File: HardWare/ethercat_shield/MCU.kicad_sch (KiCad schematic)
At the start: 49 parts, among them J2 Conn_01x03, J3 Conn_01x04, J6 Conn_01x03, J7 Conn_01x04, SW1 SW_Push, U5 STM32F407VETx, U6 TJA1051T-3, U7 TJA1051T-3, Y1 8M, Y2 32.768KHz

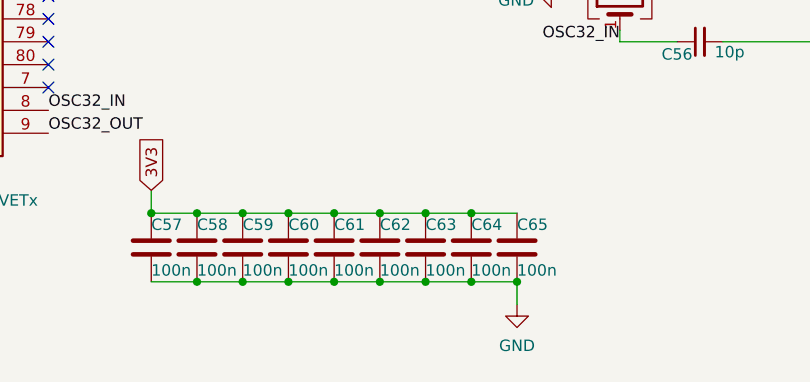
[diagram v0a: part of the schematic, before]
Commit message: 'ethercat_shield' PCB_layout completed
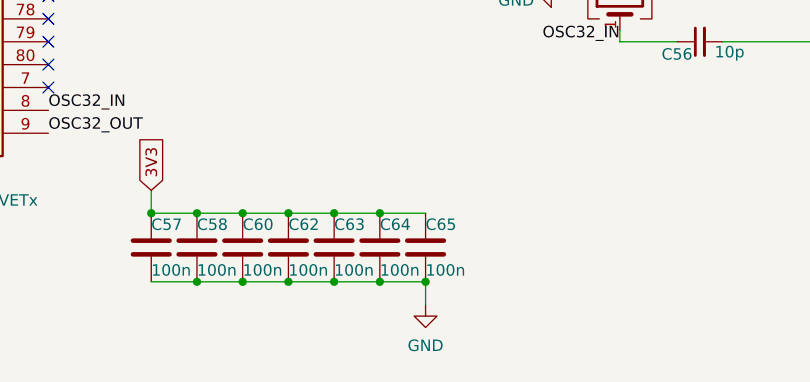
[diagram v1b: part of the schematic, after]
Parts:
- removed C59, C61: 100n, Capacitor_SMD:C_0603_1608Metric, symbol Device:C
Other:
- moved on the sheet: C60, C62, C63, C64, C65
